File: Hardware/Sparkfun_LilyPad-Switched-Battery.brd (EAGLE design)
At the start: 31.7 x 30.1 mm, 13 parts

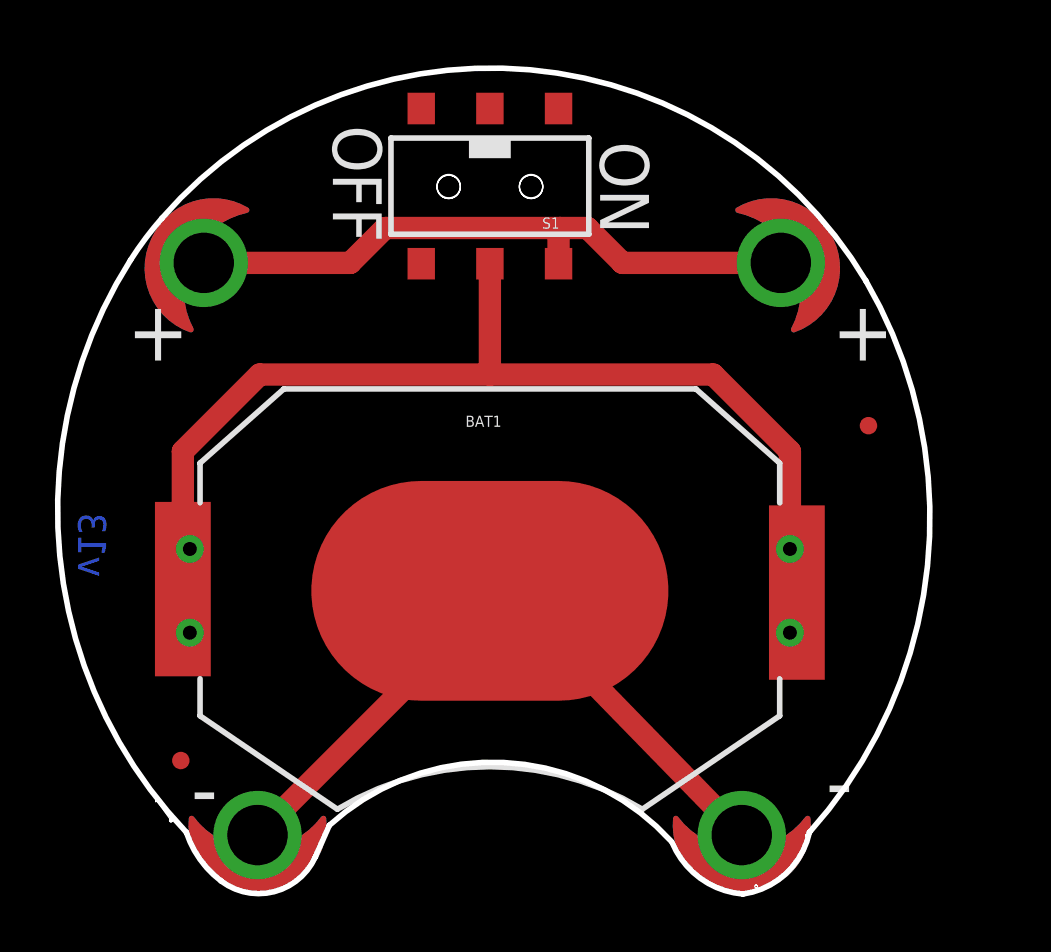
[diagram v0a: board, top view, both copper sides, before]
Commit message: Fixed DRC errors
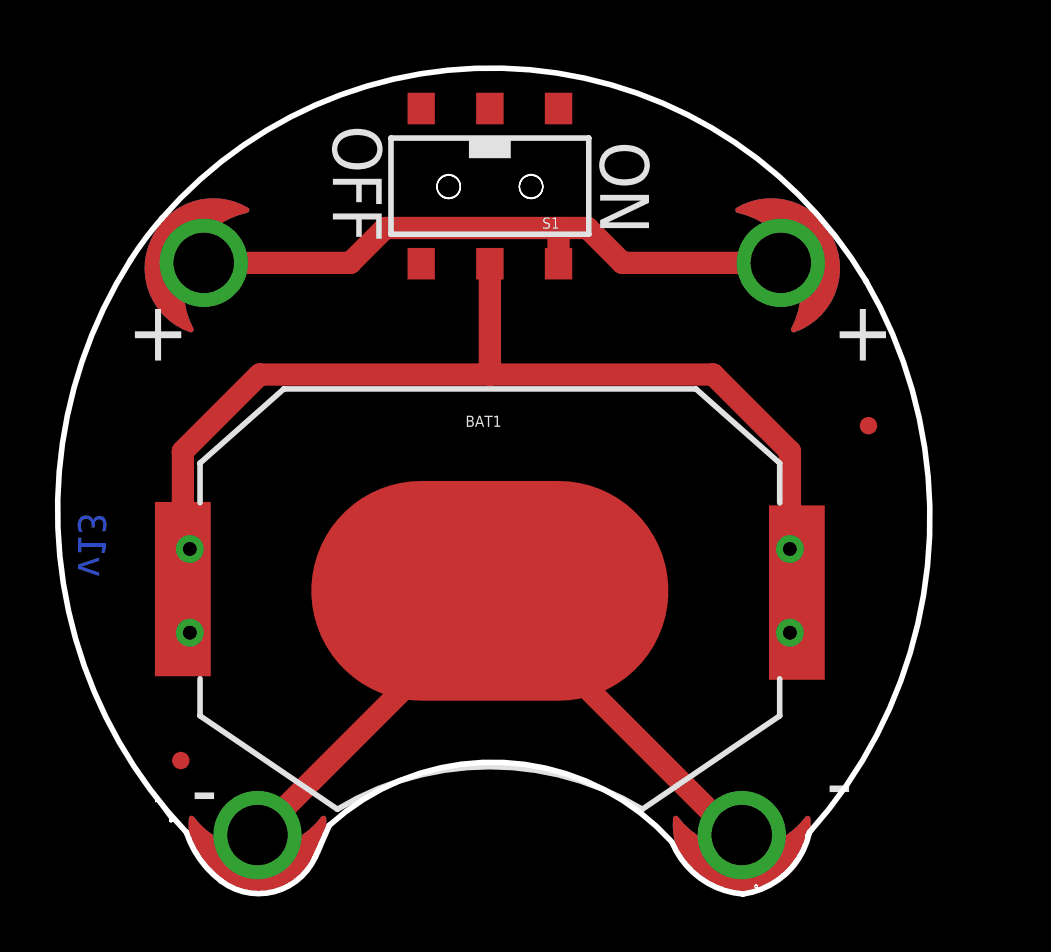
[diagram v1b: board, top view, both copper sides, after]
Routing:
- net N$1: track 44.2 -> 46.5 mm
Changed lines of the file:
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@@
 <param name="dpGapFactor" value="2.5"/>
 <param name="checkGrid" value="0"/>
-<param name="checkAngle" value="0"/>
+<param name="checkAngle" value="1"/>
 <param name="checkFont" value="1"/>
 <param name="checkRestrict" value="1"/>
@@
 <via x="24.638" y="12.446" extent="1-16" drill="0.508"/>
 <via x="24.638" y="9.398" extent="1-16" drill="0.508"/>
-<wire x1="2.794" y1="12.446" x2="2.794" y2="9.398" width="0.8128" layer="1"/>
 <wire x1="5.334" y1="18.796" x2="13.716" y2="18.796" width="0.8128" layer="1"/>
 <wire x1="13.716" y1="18.796" x2="21.844" y2="18.796" width="0.8128" layer="1"/>
-<wire x1="24.638" y1="12.446" x2="24.892" y2="9.271" width="0.8128" layer="1"/>
-<wire x1="24.638" y1="9.398" x2="24.892" y2="9.271" width="0.8128" layer="1"/>
-<wire x1="2.54" y1="12.573" x2="2.794" y2="12.446" width="0.8128" layer="1"/>
 <wire x1="2.794" y1="9.398" x2="2.54" y2="9.398" width="0.8128" layer="1"/>
 <wire x1="13.716" y1="22.829" x2="13.716" y2="18.796" width="0.8128" layer="1"/>
 <wire x1="24.892" y1="12.446" x2="24.638" y2="12.446" width="0.254" layer="1"/>
 <wire x1="5.334" y1="18.796" x2="2.54" y2="16.002" width="0.8128" layer="1"/>
-<wire x1="2.54" y1="16.002" x2="2.54" y2="12.573" width="0.8128" layer="1"/>
 <wire x1="2.54" y1="12.573" x2="2.54" y2="12.192" width="0.8128" layer="1"/>
 <wire x1="2.54" y1="12.192" x2="2.286" y2="11.938" width="0.8128" layer="1"/>
 <wire x1="2.286" y1="11.938" x2="2.286" y2="12.319" width="0.8128" layer="1"/>
-<wire x1="2.286" y1="12.319" x2="2.54" y2="12.573" width="0.8128" layer="1"/>
 <wire x1="21.844" y1="18.796" x2="24.638" y2="16.002" width="0.8128" layer="1"/>
-<wire x1="24.638" y1="16.002" x2="24.638" y2="12.446" width="0.8128" layer="1"/>
+<wire x1="2.54" y1="16.002" x2="2.54" y2="12.573" width="0.8128" layer="1"/>
+<wire x1="2.794" y1="9.398" x2="2.794" y2="12.319" width="0.8128" layer="1"/>
+<wire x1="2.794" y1="12.319" x2="2.54" y2="12.573" width="0.8128" layer="1"/>
+<wire x1="2.794" y1="12.319" x2="2.794" y2="12.446" width="0.8128" layer="1"/>
+<wire x1="24.638" y1="12.446" x2="24.638" y2="16.002" width="0.8128" layer="1"/>
+<wire x1="24.638" y1="9.398" x2="24.638" y2="12.446" width="0.8128" layer="1"/>
+<wire x1="24.638" y1="9.398" x2="24.892" y2="9.398" width="0.8128" layer="1"/>
+<wire x1="24.892" y1="9.398" x2="25.4" y2="8.89" width="0.8128" layer="1"/>
+<wire x1="25.4" y1="8.89" x2="25.4" y2="9.779" width="0.8128" layer="1"/>
+<wire x1="25.4" y1="10.16" x2="25.4" y2="9.779" width="0.8128" layer="1"/>
+<wire x1="25.4" y1="9.779" x2="24.892" y2="9.271" width="0.8128" layer="1"/>
 </signal>
 <signal name="N$2">
@@
 <contactref element="BAT1" pad="NEGATIVE"/>
 <wire x1="13.716" y1="10.922" x2="13.716" y2="10.4902" width="0.8128" layer="1"/>
-<wire x1="13.716" y1="10.922" x2="14.224" y2="10.922" width="0.8128" layer="1"/>
-<wire x1="14.224" y1="10.922" x2="22.8854" y2="2.032" width="0.8128" layer="1"/>
 <wire x1="13.716" y1="10.4902" x2="5.2578" y2="2.032" width="0.8128" layer="1"/>
+<wire x1="22.8854" y1="2.032" x2="22.606" y2="2.032" width="0.8128" layer="1"/>
+<wire x1="22.606" y1="2.032" x2="13.716" y2="10.922" width="0.8128" layer="1"/>
 </signal>
 </signals>

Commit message: Panel v13b - added inner tabs
Added inner tabs for more points of contact, which makes a stronger panel.
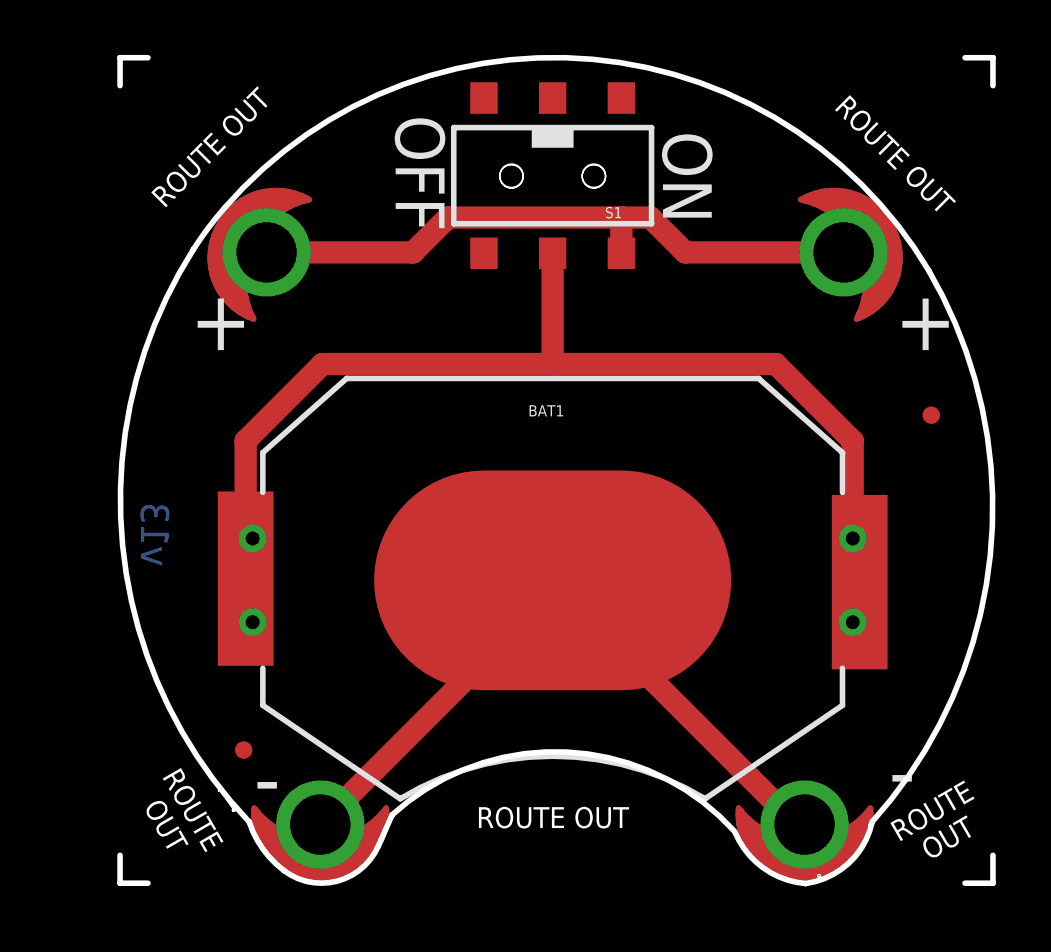
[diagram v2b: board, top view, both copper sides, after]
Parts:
- moved BATT+2 2.32 mm to (26.6, 23.2)
- moved LOGO2 2.32 mm to (21.8, 26.2)
- moved FD2 2.32 mm to (4.75, 5.13)
- moved BATB- 2.32 mm to (7.54, 2.41)
- moved BATT+ 2.32 mm to (5.59, 23.2)
- moved U$1 2.32 mm to (2.42, -12.0)
- moved BAT1 2.32 mm to (16.0, 11.3)
- moved FRAME1 2.32 mm to (-8.97, -9.42)
- moved LOGO1 2.32 mm to (11.6, 24.8)
- moved S1 2.32 mm to (16.0, 26.0)
- moved U$3 2.32 mm to (15.8, 14.9)
- moved BATB-2 2.32 mm to (25.2, 2.41)
- moved FD1 2.32 mm to (29.8, 17.3)
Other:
- board size 31.7 x 30.1 mm -> 31.8 x 30.1 mm
- board text added: "Board Thickness: 0.8mm"
- board text added: "ROUTE OUT"
- board text removed: "Board Thickness: 0.032""
